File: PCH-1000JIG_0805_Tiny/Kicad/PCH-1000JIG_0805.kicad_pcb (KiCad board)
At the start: 2 copper layers, 23.1 x 11.3 mm, 14 parts

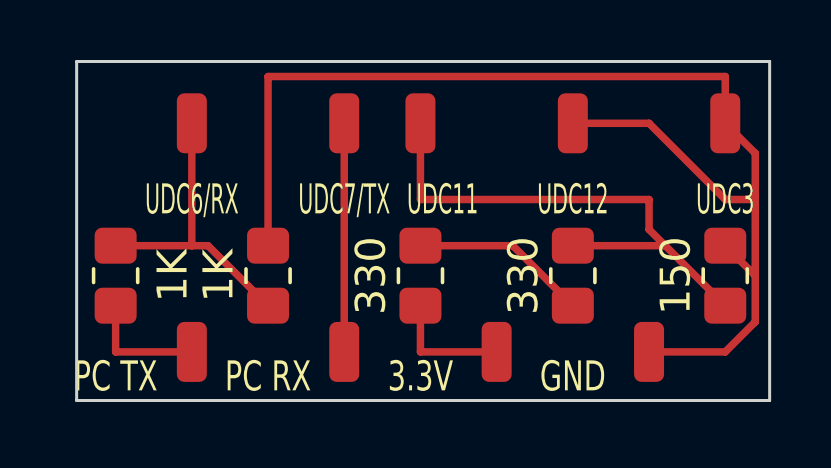
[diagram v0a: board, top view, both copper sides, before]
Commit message: moved a footprint for better clearance
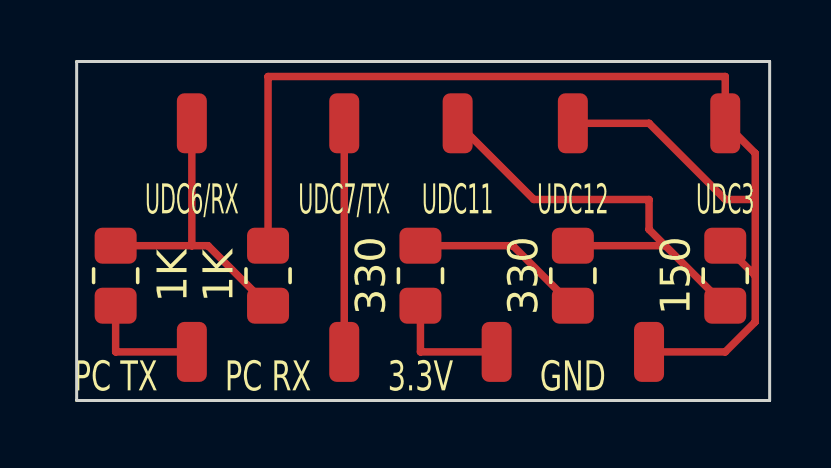
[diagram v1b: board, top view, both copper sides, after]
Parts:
- moved UDC11 1.24 mm to (49.5, 35.6)
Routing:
- net (no net): track 91.5 -> 88.8 mm
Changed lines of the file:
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@@
   )
   (footprint "Connector_Wire:SolderWirePad_1x01_SMD_1x2mm" (layer "F.Cu")
-    (at 48.26 35.56)
-    (descr "Wire Pad, Square, SMD Pad,  1mm x 2mm,")
-    (tags "MesurementPoint Square SMDPad 1mmx2mm ")
-    (attr exclude_from_pos_files exclude_from_bom)
-    (fp_text reference "UDC11" (at 0.74 2.54) (layer "F.SilkS")
+    (at 49.5 35.56)
+    (descr "Wire Pad, Square, SMD Pad,  1mm x 2mm,")
+    (tags "MesurementPoint Square SMDPad 1mmx2mm ")
+    (attr exclude_from_pos_files exclude_from_bom)
+    (fp_text reference "UDC11" (at 0 2.54) (layer "F.SilkS")
         (effects (font (size 1 0.5) (thickness 0.15)))
     )
@@
   (segment (start 59.42 40.64) (end 59.42 42.18) (width 0.25) (layer "F.Cu") (net 0))
   (segment (start 59.42 38.1) (end 59.42 40.64) (width 0.25) (layer "F.Cu") (net 0))
+  (segment (start 52.04 38.1) (end 49.5 35.56) (width 0.25) (layer "F.Cu") (net 0))
   (segment (start 55.88 39.1) (end 55.88 38.1) (width 0.25) (layer "F.Cu") (net 0))
   (segment (start 40.64 39.64) (end 40.64 35.56) (width 0.25) (layer "F.Cu") (net 0))
-  (segment (start 55.88 38.1) (end 48.26 38.1) (width 0.25) (layer "F.Cu") (net 0))
   (segment (start 48.26 39.64) (end 51.34 39.64) (width 0.25) (layer "F.Cu") (net 0))
   (segment (start 43.18 39.64) (end 43.18 34) (width 0.25) (layer "F.Cu") (net 0))
@@
   (segment (start 55.88 35.56) (end 58.42 38.1) (width 0.25) (layer "F.Cu") (net 0))
   (segment (start 41.18 39.64) (end 43.18 41.64) (width 0.25) (layer "F.Cu") (net 0))
-  (segment (start 48.26 38.1) (end 48.26 35.56) (width 0.25) (layer "F.Cu") (net 0))
   (segment (start 56.42 39.64) (end 55.88 39.1) (width 0.25) (layer "F.Cu") (net 0))
   (segment (start 45.72 35.56) (end 45.72 43.18) (width 0.25) (layer "F.Cu") (net 0))
+  (segment (start 55.88 38.1) (end 52.04 38.1) (width 0.25) (layer "F.Cu") (net 0))
   (segment (start 48.26 41.64) (end 48.26 43.18) (width 0.25) (layer "F.Cu") (net 0))
   (segment (start 58.42 38.1) (end 59.42 38.1) (width 0.25) (layer "F.Cu") (net 0))
